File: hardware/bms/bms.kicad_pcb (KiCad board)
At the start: 4 copper layers, 120 x 45 mm, 273 parts, among them J1 Screw_Terminal_01x01, J10 Conn_01x10, J11 USB_C_Receptacle_USB2.0, J12 Conn_01x03, J13 Conn_01x07, J2 Screw_Terminal_01x01, J3 Screw_Terminal_01x01, J4 Screw_Terminal_01x01, J5 Screw_Terminal_01x01, J6 Conn_01x02, J7 Conn_01x10, J8 Conn_01x02, J9 Micro_SD_Card_Det2, Q1 MMBT3904, Q2 Q_PMOS_GSD, Q3 Q_PMOS_GSD, Q4 BSZ018N04LS6ATMA1, Q5 IAUC120N04S6N006ATMA1, Q6 IAUC120N04S6N006ATMA1, Q7 BSZ018N04LS6ATMA1, Q8 BSZ018N04LS6ATMA1, Q9 BSZ018N04LS6ATMA1, SW1 SW_SPST, SW2 SW_Push, SW3 SW_Push, U1 BQ76952, U2 LM74700, U3 BQ24610, U4 LM5166X, U5 TPS62172DSG, U6 ESP32-C3-MINI-1-N4, U7 SN74LXC1T14DCKR, U8 USBLC6-2SC6

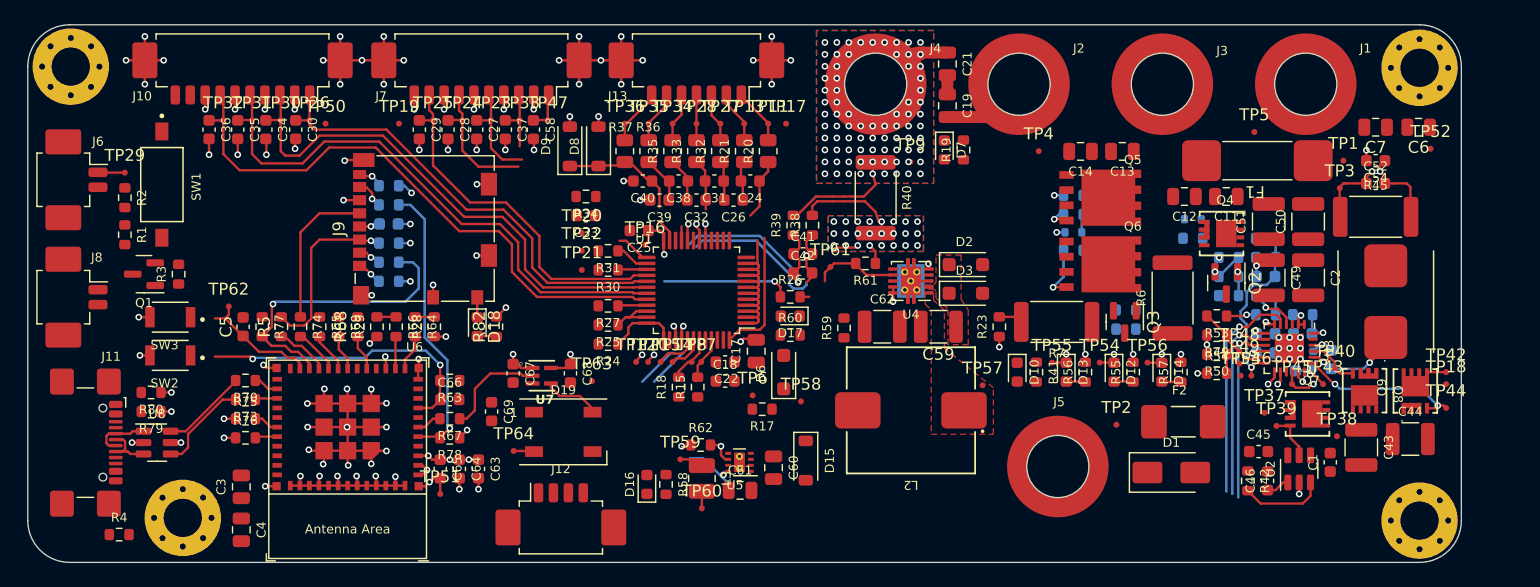
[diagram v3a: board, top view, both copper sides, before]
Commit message: Power plane and thermal vias for charger and FETs section
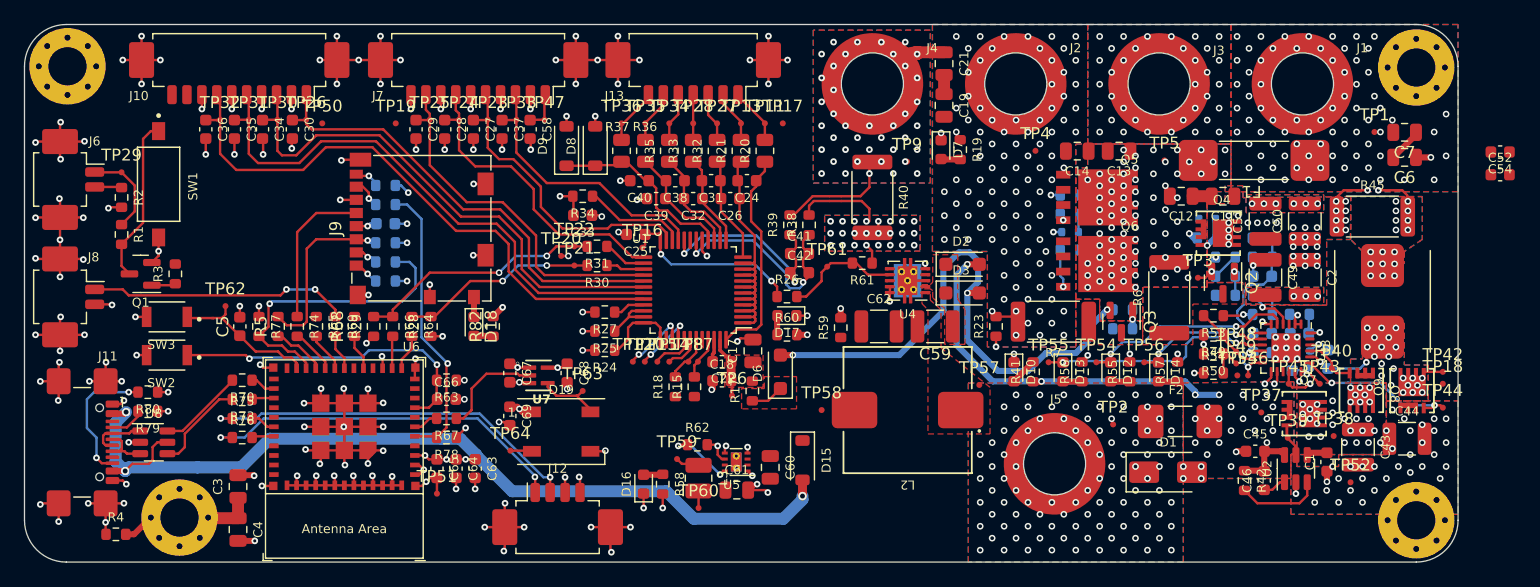
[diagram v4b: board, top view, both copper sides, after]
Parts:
- moved TP52 28.7 mm to (199.5, 113.3)
- moved TP3 14.0 mm to (186.7, 96.2)
- moved C52 10.5 mm to (212.0, 87.6)
- moved C54 10.5 mm to (212.0, 85.7)
- moved TP5 7.89 mm to (183.9, 86.4)
- moved TP1 3.54 mm to (201.5, 84.0)
- moved C6 2.78 mm to (204.0, 86.1)
- moved TP20 2.58 mm to (133.4, 94.4)
- moved C7 2.46 mm to (204.0, 84.0)
- moved TP58 1.87 mm to (155.2, 107.3)
- moved R17 1.73 mm to (149.4, 105.7), turned to 90 degrees
- moved TP6 1.73 mm to (147.7, 106.1)
- moved C69 1.57 mm to (129.1, 107.8)
- moved NT4 1.40 mm to (202.3, 88.9)
- moved TP39 1.37 mm to (194.2, 109.6)
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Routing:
- net GND: track 157.7 -> 249.3 mm, vias 126 -> 267
- net /VUSB_5V: track 0.86 -> 76.3 mm, vias 1 -> 3
- net /VBAT_IN_F: track 0.00 -> 48.4 mm, vias 0 -> 78
- net /VCHG_IN_F: track 0.00 -> 39.2 mm, vias 0 -> 23
- net /MCU/UART_RX: track 0.97 -> 32.2 mm, vias 1 -> 2
- net /MCU/UART_TX: track 0.97 -> 31.3 mm, vias 1 -> 2
- net /MCU/PWM_OUT: track 0.00 -> 21.8 mm, vias 0 -> 2
- net /BATTERY BALANCE AND MONITOR/I2C_SCL: track 1.60 -> 20.6 mm, vias 0 -> 2
- net /THERM_0: track 6.23 -> 22.7 mm
- net /BATTERY BALANCE AND MONITOR/I2C_SDA: track 1.60 -> 16.4 mm, vias 0 -> 2
- net /THERM_1: track 10.2 -> 25.0 mm
- net Net-(Q1-C): track 0.00 -> 13.9 mm
- net /THERM_2: track 13.9 -> 25.9 mm
- net Net-(J11-CC2): track 0.00 -> 11.3 mm, vias 0 -> 2
- net /BATTERY BALANCE AND MONITOR/TS2: track 0.00 -> 8.63 mm
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- added copper zone on B.Cu, net /BATTERY BALANCE AND MONITOR/PACK+
- added copper zone on F.Cu, net /BATTERY BALANCE AND MONITOR/PACK+
- added copper zone on In2.Cu, net /BATTERY BALANCE AND MONITOR/PACK+
- added copper zone on B.Cu, net /BATTERY BALANCE AND MONITOR/VCHG+
- added copper zone on F.Cu, net /BATTERY BALANCE AND MONITOR/VCHG+
- added copper zone on In2.Cu, net /BATTERY BALANCE AND MONITOR/VCHG+
- added copper zone on B.Cu, net /BATTERY CHARGER/CHG_IN_PROT
- added copper zone on F.Cu, net /BATTERY CHARGER/CHG_IN_PROT
- added copper zone on In2.Cu, net /BATTERY CHARGER/CHG_IN_PROT
- added copper zone on B.Cu, net /BATTERY CHARGER/SW_NODE
- added copper zone on F.Cu, net /BATTERY CHARGER/SW_NODE
- added copper zone on B.Cu, net /VBAT_IN
- added copper zone on F.Cu, net /VBAT_IN
- added copper zone on In1.Cu, net /VBAT_IN
- added copper zone on In2.Cu, net /VBAT_IN
- added copper zone on B.Cu, net /VBAT_IN_F
- added copper zone on F.Cu, net /VBAT_IN_F
- added copper zone on In2.Cu, net /VBAT_IN_F
- added copper zone on B.Cu, net /VCHG_IN
- added copper zone on F.Cu, net /VCHG_IN
- added copper zone on In1.Cu, net /VCHG_IN
- added copper zone on In2.Cu, net /VCHG_IN
- added copper zone on B.Cu, net /VCHG_IN_F
- added copper zone on F.Cu, net /VCHG_IN_F
- added copper zone on In2.Cu, net /VCHG_IN_F
- added copper zone on F.Cu, net Net-(D6-K)
- added copper zone on B.Cu, net Net-(L1-Pad2)
- added copper zone on F.Cu, net Net-(L1-Pad2)
- added copper zone on In2.Cu, net Net-(L1-Pad2)
- added copper zone on F.Cu, net Net-(Q2-D)
- added copper zone on F.Cu, net Net-(Q3-D)
- added copper zone on F.Cu, net Net-(U1-BAT)

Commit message: Few cross-board connections made, a bit tricky to work around power planes
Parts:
- C52, C54: moved to B.Cu
- moved C54 29.4 mm to (189.0, 104.0)
- moved C52 25.8 mm to (192.1, 104.0)
- moved TP53 0.12 mm to (189.9, 104.4)
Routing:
- net /VCHG_IN_F: track 39.2 -> 115.6 mm
- net /THERM_CHG: track 5.27 -> 64.9 mm, vias 1 -> 3
- net /BMS_WAKE: track 10.2 -> 49.9 mm, vias 1 -> 2
- net /CHG_STAT1: track 17.8 -> 49.3 mm, vias 2 -> 3
- net /BATTERY CHARGER/VREF: track 12.0 -> 41.4 mm
- net /CHG_STAT2: track 19.6 -> 42.7 mm, vias 2 -> 3
- net /BATTERY BALANCE AND MONITOR/PACK: track 3.02 -> 23.0 mm, vias 1 -> 2
- net /BATTERY BALANCE AND MONITOR/CGATE: track 3.28 -> 22.9 mm, vias 1 -> 2
- net /BATTERY BALANCE AND MONITOR/LD: track 4.38 -> 17.9 mm, vias 1 -> 2
- net /BATTERY CHARGER/SRP_CHG: track 21.4 -> 26.7 mm
- net /BATTERY CHARGER/SRN_CHG: track 21.2 -> 22.3 mm
- net /BATTERY BALANCE AND MONITOR/DGATE: track 4.70 -> 5.58 mm, vias 0 -> 1
- net +5V: track 5.99 -> 6.84 mm

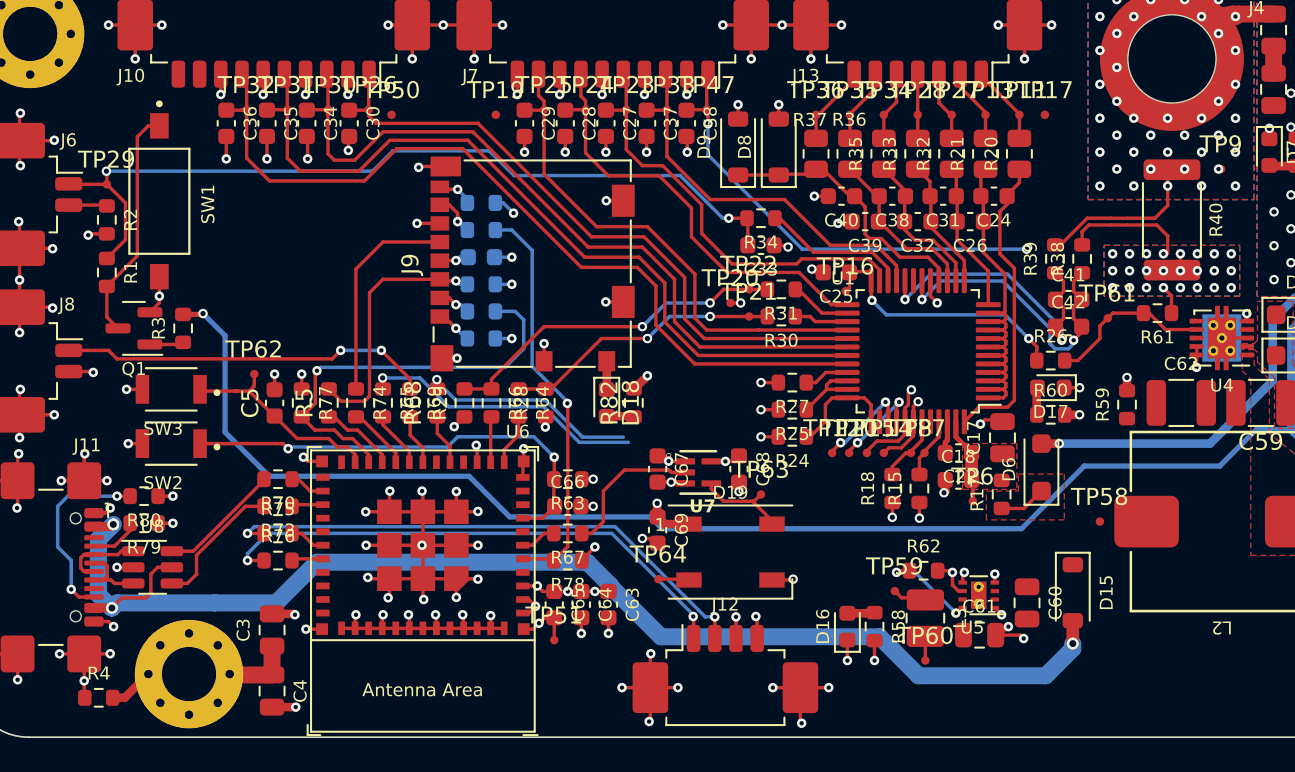
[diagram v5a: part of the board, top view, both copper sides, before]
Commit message: Added extra features to try and prevent SD card data corruption. Added override enable so that the MCU can keep itself on until the SD card is finished writing, also added 5V / wake detect circuit so the MCU can begin to sense when the 5V rail is dropping and react accordingly
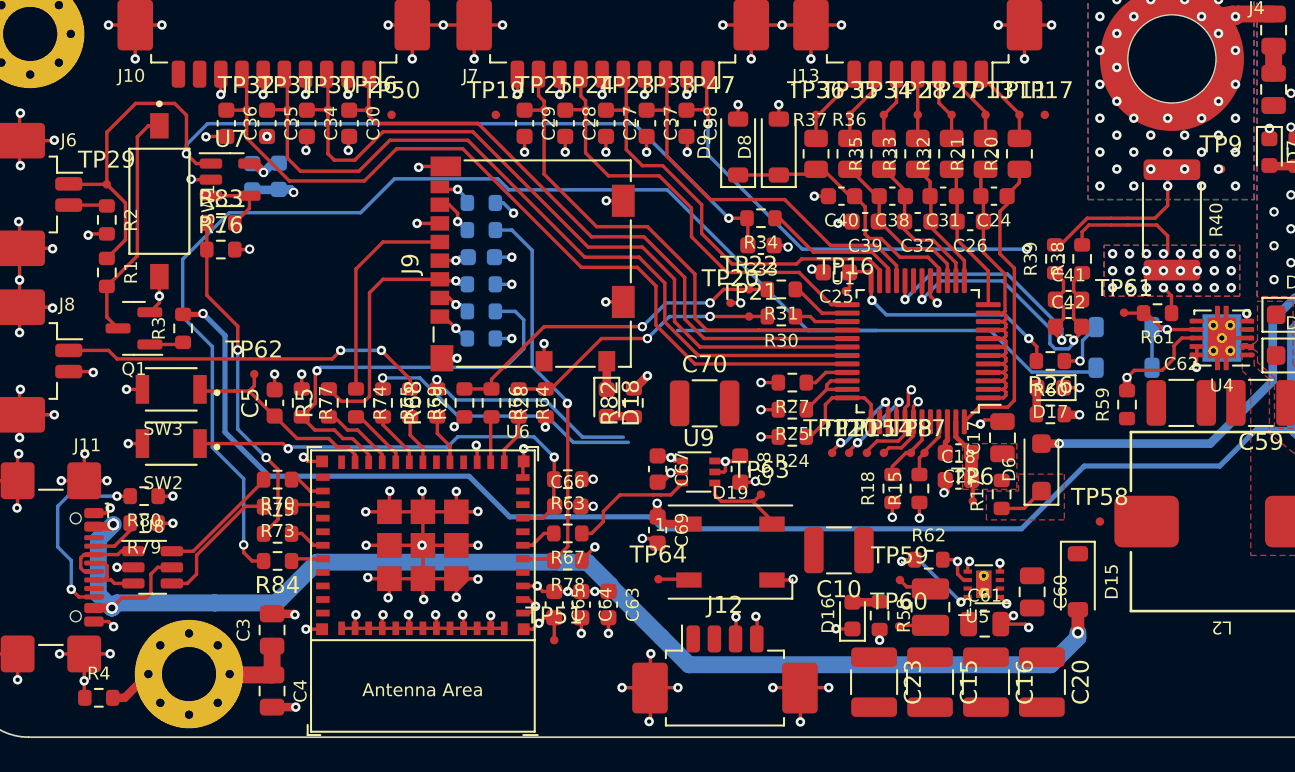
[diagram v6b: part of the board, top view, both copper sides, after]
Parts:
- added C10: 100uF, Capacitor_SMD:C_1210_3225Metric, F.Cu at (139.8, 109.0)
- added C15: 100uF, Capacitor_SMD:C_1210_3225Metric, F.Cu at (145.2, 116.8)
- added C16: 100uF, Capacitor_SMD:C_1210_3225Metric, F.Cu at (148.5, 116.8)
- added C20: 100uF, Capacitor_SMD:C_1210_3225Metric, F.Cu at (151.8, 116.8)
- added C23: 100uF, Capacitor_SMD:C_1210_3225Metric, F.Cu at (141.9, 116.8)
- added C70: 100uF, Capacitor_SMD:C_1210_3225Metric, F.Cu at (131.9, 100.3)
- added C71: 1uF, Capacitor_SMD:C_0603_1608Metric, B.Cu at (106.8, 86.9)
- added C9: 0.1uF, Capacitor_SMD:C_0603_1608Metric, B.Cu at (105.2, 86.9)
- added D20: D_Schottky, Diode_SMD:D_SOD-123, B.Cu at (156.7, 95.8)
- added D21: D_Schottky, Diode_SMD:D_SOD-123, B.Cu at (156.7, 98.2)
- added R83: 5.1k, Resistor_SMD:R_0603_1608Metric, F.Cu at (103.3, 89.7)
- added R84: 1k, Resistor_SMD:R_0603_1608Metric, F.Cu at (106.7, 109.6)
- added U9: TXU0101DCKR, Package_TO_SOT_SMD:SOT-363_SC-70-6, F.Cu at (131.6, 104.3)
- R26: value 0R -> 1k
- R61: value 100k -> 1.5M
- R76: value 0R -> 10k
- U7: value SN74LXC1T14DCKR -> MCP6001U; footprint bms:DCK0005A-IPC_C -> Package_TO_SOT_SMD:SOT-23-5
- moved U7 32.6 mm to (103.9, 87.1)
- moved R76 18.7 mm to (103.3, 91.2)
- moved TP60 2.55 mm to (143.4, 113.5)
- moved TP61 1.02 mm to (156.7, 95.0)
- moved TP59 0.72 mm to (143.4, 110.7)
- moved U5 0.72 mm to (148.4, 111.0)
- moved C60 0.72 mm to (151.2, 111.4)
- moved C61 0.72 mm to (148.4, 113.3)
- moved D15 0.72 mm to (153.9, 110.8)
- moved D16 0.72 mm to (140.6, 112.8)
- moved L3 0.72 mm to (145.2, 112.3)
- moved R58 0.72 mm to (142.2, 112.8)
- moved R62 0.72 mm to (145.1, 109.5)
- moved C68 0.08 mm to (134.0, 104.2)
- turned R26 to 180 degrees
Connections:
- net /MCU/RXD0 renamed /MCU/GPIO20
- J12 pad 1: /MCU/UART_TX -> /BATTERY BALANCE AND MONITOR/I2C_SDA
- J12 pad 2: /MCU/UART_RX -> /BATTERY BALANCE AND MONITOR/I2C_SCL
- R26 pad 1: /BATTERY BALANCE AND MONITOR/REG18 -> /BATTERY BALANCE AND MONITOR/PWR_EN
- R26 pad 2: /BATTERY BALANCE AND MONITOR/PWR_EN -> /BATTERY BALANCE AND MONITOR/REG18
- R61 pad 2: /BATTERY BALANCE AND MONITOR/PWR_EN -> /MCU/5V_EN
- R75 pad 1: /MCU/UART_RX -> /MCU/WAKE_DETECT
- R76 pad 1: /MCU/UART_TX -> /MCU/WAKE_DETECT
- R76 pad 2: /MCU/TXD0 -> GND
- TP61 pad 1: /BATTERY BALANCE AND MONITOR/PWR_EN -> /MCU/5V_EN
- U4 pad 7: /BATTERY BALANCE AND MONITOR/PWR_EN -> /MCU/5V_EN
- U6 pad 31: /MCU/TXD0 -> /MCU/GPIO21
- U7 pad 1: +3V3 -> /BMS_WAKE
- U7 pad 2: /MCU/RGB_DIN_ESP -> GND
- U7 pad 3: GND -> /MCU/OP_OUT_WAKE
- U7 pad 4: /MCU/RGB_DIN -> /MCU/OP_OUT_WAKE
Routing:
- net /MCU/SD_CARD_WRITE: track 0.00 -> 92.6 mm, vias 0 -> 1
- net /MCU/UART_RX: track 32.2 -> 0.00 mm, vias 2 -> 0
- net /MCU/UART_TX: track 31.6 -> 0.00 mm, vias 2 -> 0
- net /MCU/WAKE_DETECT: track 0.00 -> 20.4 mm, vias 0 -> 2
- net +5V: track 6.84 -> 16.4 mm, vias 4 -> 5
- net /BMS_WAKE: track 49.9 -> 58.3 mm
- net /MCU/5V_EN: track 0.00 -> 7.78 mm, vias 0 -> 1
- net /BATTERY BALANCE AND MONITOR/PWR_EN: track 9.50 -> 3.32 mm, vias 0 -> 1
- net /MCU/OP_OUT_WAKE: track 0.00 -> 4.23 mm
- net GND: track 249.6 -> 252.4 mm, vias 267 -> 270
- net /MCU/TXD0: track 1.87 -> 0.00 mm
- net /MCU/GPIO21: track 0.00 -> 1.87 mm
- net /MCU/RGB_DIN_ESP: track 8.77 -> 7.64 mm
- net +3V3: track 25.1 -> 24.4 mm
- net /THERM_7: track 49.4 -> 48.7 mm

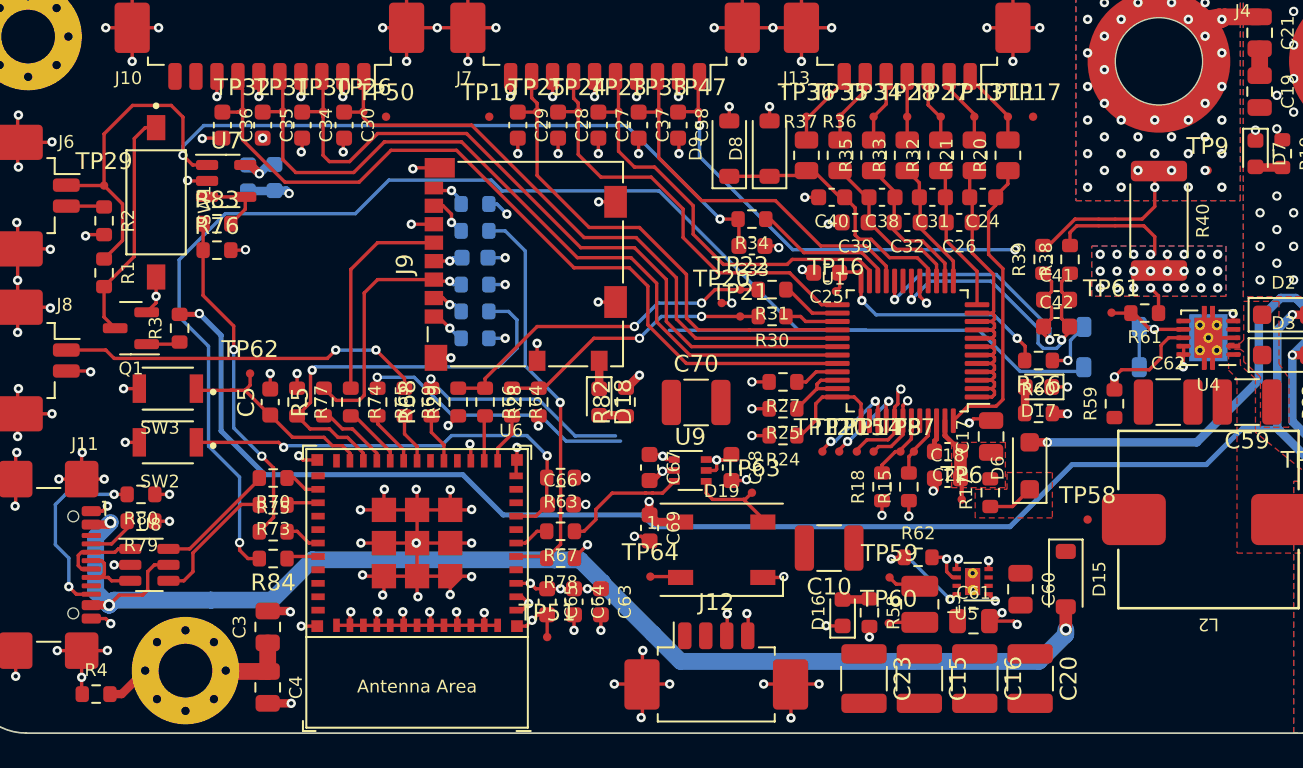
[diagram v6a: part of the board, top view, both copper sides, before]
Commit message: Added bulk cap for 5V and 3V3 rails, made sure they fit in current layout
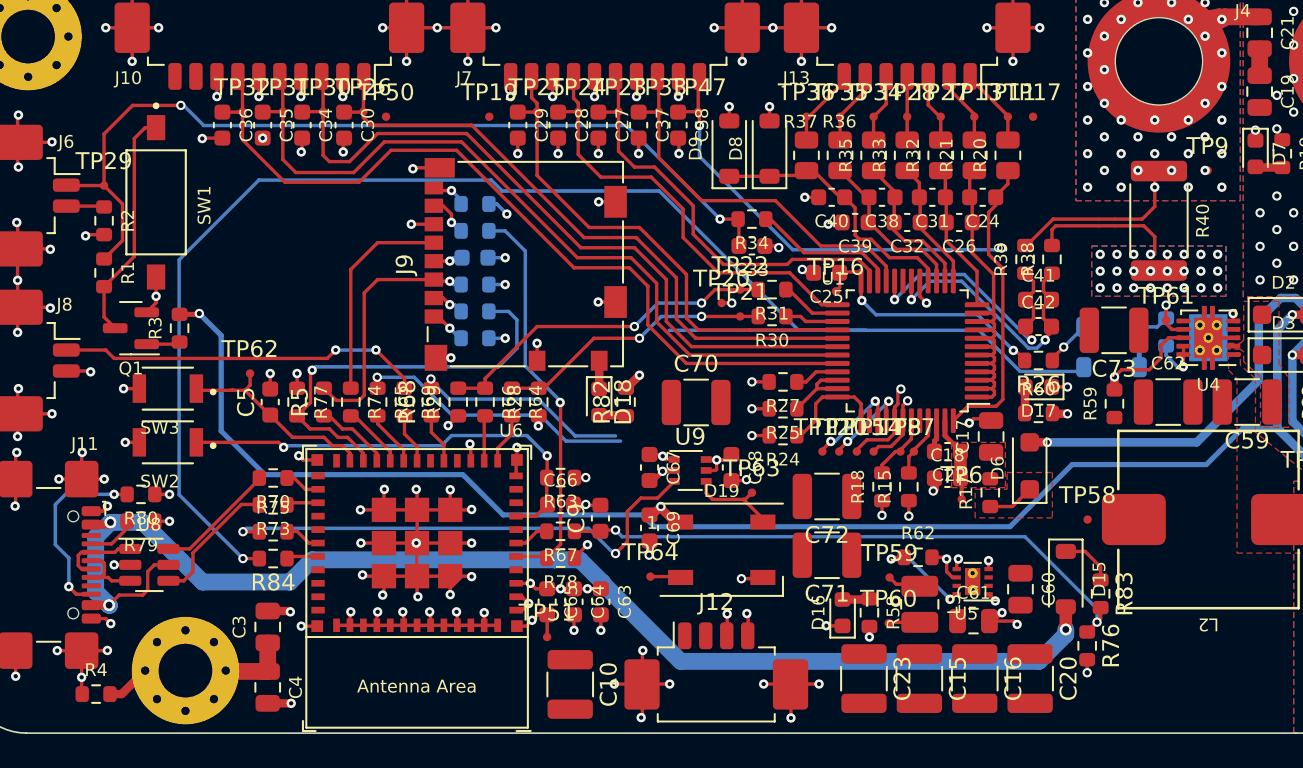
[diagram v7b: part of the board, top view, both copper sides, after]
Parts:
- removed U7: MCP6001U, Package_TO_SOT_SMD:SOT-23-5
- added C72: 100uF, Capacitor_SMD:C_1210_3225Metric, F.Cu at (139.7, 105.9)
- added C73: 100uF, Capacitor_SMD:C_1210_3225Metric, F.Cu at (156.8, 96.0)
- C71: value 1uF -> 100uF; footprint Capacitor_SMD:C_0603_1608Metric -> Capacitor_SMD:C_1210_3225Metric; moved to F.Cu
- C9: moved to F.Cu
- R61: moved to B.Cu
- R83: value 5.1k -> 10k
- moved R83 57.1 mm to (156.0, 111.7), turned to -90 degrees
- moved R76 57.0 mm to (155.2, 114.8), turned to -90 degrees
- moved C71 39.9 mm to (139.7, 109.4), turned to 180 degrees
- moved C9 29.2 mm to (126.2, 107.2), turned to 90 degrees
- moved C10 17.4 mm to (124.4, 117.1), turned to -90 degrees
- moved TP61 3.28 mm to (159.9, 95.4)
- moved R61 1.70 mm to (159.9, 96.1), turned to 90 degrees
- moved C41 1.07 mm to (152.3, 94.2)
- moved C42 1.07 mm to (152.3, 95.8)
- moved R38 1.07 mm to (153.1, 91.8)
- moved R39 1.07 mm to (151.5, 91.8)
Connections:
- C9 pad 1: +5V -> /MCU/5V_DETECT
- R67 pad 1: /MCU/RGB_DIN_ESP -> /MCU/5V_DETECT
- R75 pad 1: /MCU/WAKE_DETECT -> /MCU/RGB_DIN_ESP
- R76 pad 1: /MCU/WAKE_DETECT -> /MCU/5V_DETECT
- R83 pad 1: /MCU/WAKE_DETECT -> +5V
- R83 pad 2: /MCU/OP_OUT_WAKE -> /MCU/5V_DETECT
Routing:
- net /MCU/5V_DETECT: track 0.00 -> 37.4 mm, vias 0 -> 2
- net /MCU/RGB_DIN_ESP: track 7.64 -> 30.3 mm, vias 0 -> 2
- net /MCU/WAKE_DETECT: track 20.4 -> 0.00 mm, vias 2 -> 0
- net /BMS_WAKE: track 58.3 -> 53.5 mm
- net /MCU/OP_OUT_WAKE: track 4.23 -> 0.00 mm
- net GND: track 252.4 -> 249.6 mm, vias 270 -> 268
- net /BATTERY BALANCE AND MONITOR/SRP: track 18.0 -> 16.4 mm
- net /BATTERY BALANCE AND MONITOR/SRN: track 17.9 -> 16.5 mm
- net Net-(NT1-Pad1): track 2.64 -> 3.82 mm
- net Net-(NT2-Pad1): track 3.95 -> 5.03 mm
- net /VUSB_5V: track 76.3 -> 77.2 mm
- net /MCU/5V_EN: track 7.78 -> 7.00 mm
- net /BATTERY BALANCE AND MONITOR/REG18: track 16.1 -> 15.4 mm
- net /BATTERY BALANCE AND MONITOR/PWR_EN: track 3.32 -> 2.78 mm
- net +5V: track 16.4 -> 16.2 mm, vias 5 -> 4
